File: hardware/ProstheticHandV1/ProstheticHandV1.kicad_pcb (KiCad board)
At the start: 2 copper layers, 119.4 x 88.9 mm, 25 parts, among them J1 Servo_01, J2 Servo_02, J3 Servo_03, J4 Servo_04, J5 JTAG, J6 Bat_Con, J7 OLED_Disp, J8 EMG_Sensor_01, J9 EMG_Sensor_02, SW1 Button_01, SW2 Button_02, U1 LM7805_TO220, U2 LM7809_TO220, U3 LM7909_TO220

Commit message: Done hand PCB v1
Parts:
- moved J6 119.6 mm to (186.4, 79.2), turned to 0 degrees
- moved R7 1.78 mm to (126.7, 113.8)
- moved J3 0.58 mm to (165.4, 78.5)
- moved J4 0.58 mm to (157.7, 78.5)
- moved J1 0.58 mm to (180.6, 78.5)
- moved J2 0.58 mm to (173.0, 78.5)
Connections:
- A2 pad 10: ServoControl_02 -> ServoControl_03
- A2 pad 11: ServoControl_01 -> ServoControl_04
- A2 pad 8: ServoControl_03 -> ServoControl_01
- A2 pad 9: ServoControl_04 -> ServoControl_02
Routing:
- net +BATT: track 64.1 -> 251.8 mm, vias 0 -> 2
- net +5V: track 0.00 -> 155.1 mm, vias 0 -> 2
- net +3V3: track 29.7 -> 181.0 mm, vias 2 -> 4
- net JTAG_TRST: track 0.00 -> 105.8 mm, vias 0 -> 2
- net ServoControl_01: track 0.00 -> 63.5 mm, vias 0 -> 2
- net ServoControl_02: track 0.00 -> 52.8 mm, vias 0 -> 2
- net JTAG_TCK: track 0.00 -> 48.2 mm, vias 0 -> 2
- net ServoControl_03: track 0.00 -> 43.6 mm, vias 0 -> 2
- net JTAG_TDI: track 0.00 -> 37.4 mm, vias 0 -> 2
- net JTAG_TMS: track 0.00 -> 35.3 mm, vias 0 -> 2
- net JTAG_TDO: track 0.00 -> 33.2 mm, vias 0 -> 2
- net ServoControl_04: track 0.00 -> 32.3 mm
- net unconnected-(A2-0-Pad31): track 0.00 -> 9.15 mm
- net unconnected-(A2-19-Pad25): track 0.00 -> 8.90 mm
- net unconnected-(A2-37-Pad34): track 0.00 -> 7.12 mm
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- added copper zone on F.Cu, net GND
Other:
- board size 119.4 x 88.9 mm -> 119.4 x 90.9 mm

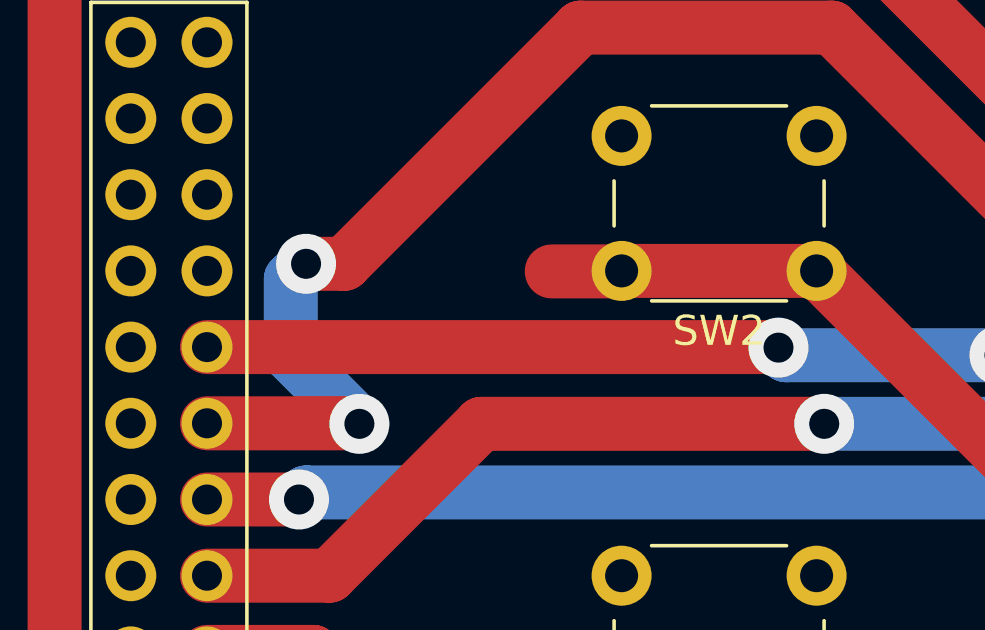
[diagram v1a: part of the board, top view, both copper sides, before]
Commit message: Update schematic: jtag fix
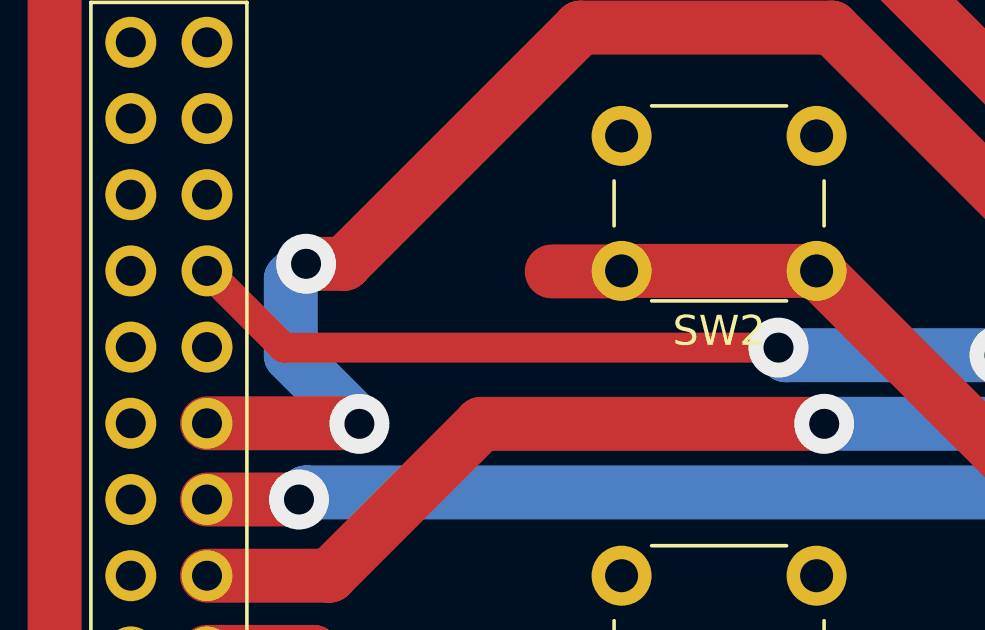
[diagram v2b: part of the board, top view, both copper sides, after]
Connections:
- J5 pad 11: JTAG_TDO -> unconnected-(J5-Pin_11-Pad11)
- J5 pad 13: unconnected-(J5-Pin_13-Pad13) -> JTAG_TDO
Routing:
- net JTAG_TDO: track 33.2 -> 34.3 mm
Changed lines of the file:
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@@
   (net 41 "Net-(D1-A)")
   (net 42 "+BATT")
-  (net 43 "unconnected-(J5-Pin_13-Pad13)")
+  (net 43 "unconnected-(J5-Pin_11-Pad11)")
   (net 44 "unconnected-(J5-Pin_15-Pad15)")
   (net 45 "unconnected-(J5-Pin_17-Pad17)")
@@
       (net 21 "GND") (pinfunction "Pin_10") (pintype "passive"))
     (pad "11" thru_hole oval (at 0 12.7 180) (size 1.7 1.7) (drill 1) (layers "*.Cu" "*.Mask")
-      (net 34 "JTAG_TDO") (pinfunction "Pin_11") (pintype "passive"))
+      (net 43 "unconnected-(J5-Pin_11-Pad11)") (pinfunction "Pin_11") (pintype "passive"))
     (pad "12" thru_hole oval (at 2.54 12.7 180) (size 1.7 1.7) (drill 1) (layers "*.Cu" "*.Mask")
       (net 21 "GND") (pinfunction "Pin_12") (pintype "passive"))
     (pad "13" thru_hole oval (at 0 15.24 180) (size 1.7 1.7) (drill 1) (layers "*.Cu" "*.Mask")
-      (net 43 "unconnected-(J5-Pin_13-Pad13)") (pinfunction "Pin_13") (pintype "passive"))
+      (net 34 "JTAG_TDO") (pinfunction "Pin_13") (pintype "passive"))
     (pad "14" thru_hole oval (at 2.54 15.24 180) (size 1.7 1.7) (drill 1) (layers "*.Cu" "*.Mask")
       (net 21 "GND") (pinfunction "Pin_14") (pintype "passive"))
@@
   (segment (start 100.312 103.36) (end 100.33 103.378) (width 1.8) (layer "F.Cu") (net 34))
   (segment (start 107.968 103.36) (end 107.696 103.632) (width 1.8) (layer "F.Cu") (net 34))
+  (segment (start 81.28 100.82) (end 83.838 103.378) (width 1) (layer "F.Cu") (net 34))
   (segment (start 114.3 103.36) (end 107.968 103.36) (width 1.8) (layer "F.Cu") (net 34))
-  (segment (start 81.28 103.36) (end 100.312 103.36) (width 1.8) (layer "F.Cu") (net 34))
+  (segment (start 83.838 103.378) (end 100.33 103.378) (width 1) (layer "F.Cu") (net 34))
   (via (at 100.33 103.378) (size 2) (drill 1) (layers "F.Cu" "B.Cu") (net 34))
   (via (at 107.696 103.632) (size 2) (drill 1) (layers "F.Cu" "B.Cu") (net 34))

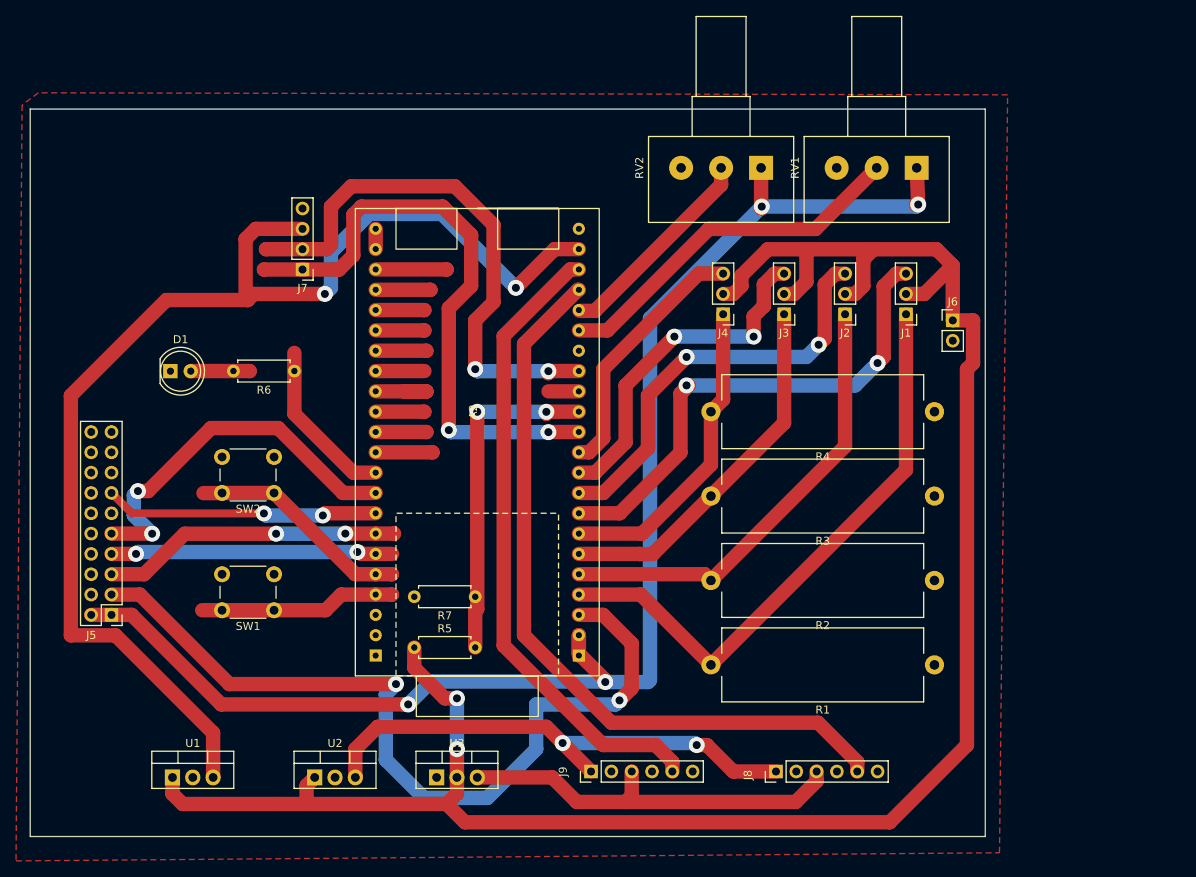
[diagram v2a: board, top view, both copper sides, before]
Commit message: Update PCB for hand, completely new design
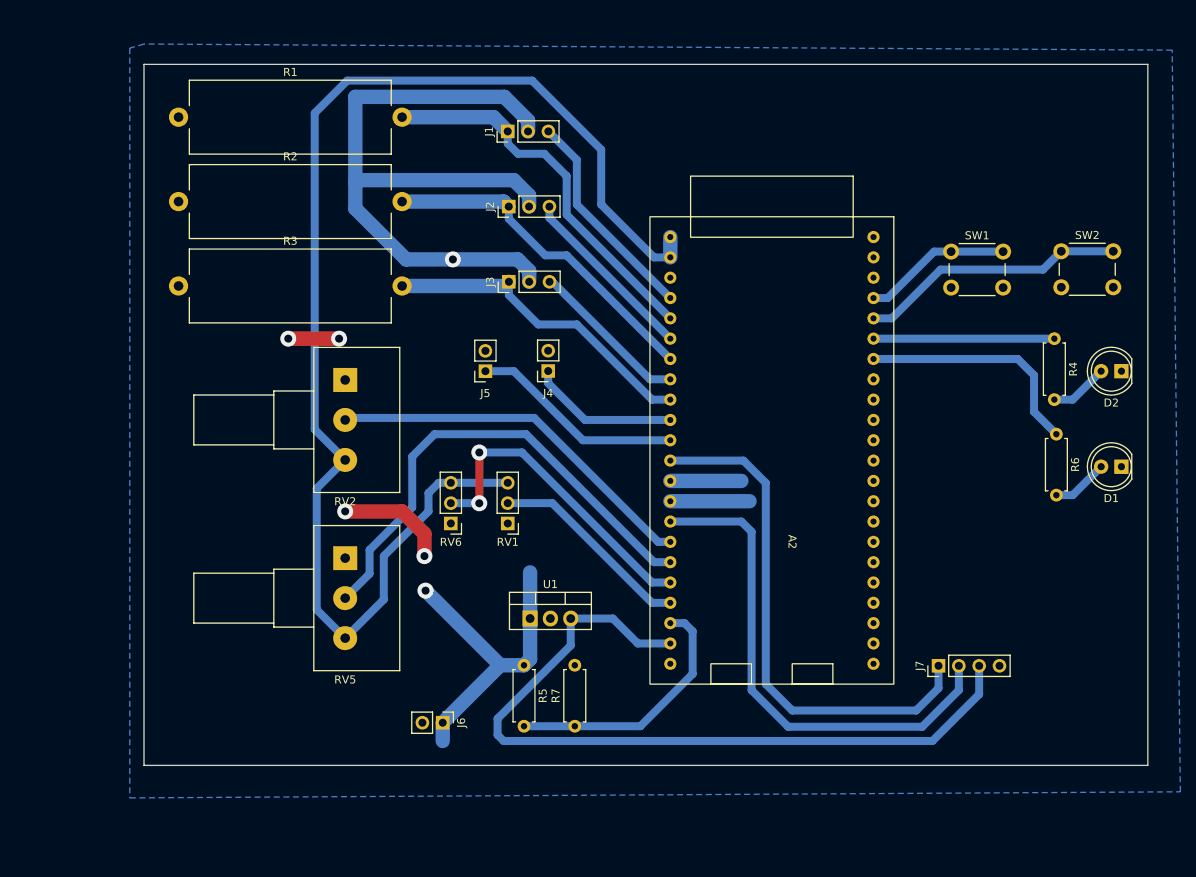
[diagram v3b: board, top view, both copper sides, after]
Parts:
- removed J8: EMG_Sensor_01, Connector_PinHeader_2.54mm:PinHeader_1x06_P2.54mm_Vertical
- removed J9: EMG_Sensor_02, Connector_PinHeader_2.54mm:PinHeader_1x06_P2.54mm_Vertical
- removed U2: LM7809_TO220, Package_TO_SOT_THT:TO-220-3_Vertical
- removed U3: LM7909_TO220, Package_TO_SOT_THT:TO-220-3_Vertical
- added D2: GREEN, LED_THT:LED_D5.0mm, F.Cu at (207.5, 85.6)
- added RV5: TrimPot_02, Potentiometer_THT:Potentiometer_Alps_RK163_Single_Horizontal, F.Cu at (110.5, 109.0)
- added RV6: TrimPot_03, Connector_PinHeader_2.54mm:PinHeader_1x03_P2.54mm_Vertical, F.Cu at (123.7, 104.6)
- A2: footprint MyLibrary:ESP32_S3_DevKitC_V1 -> FootprintLibrary:ESP32S3_DevModule
- J4: value Servo_04 -> EMG_Sensor_01; footprint Connector_PinHeader_2.54mm:PinHeader_1x03_P2.54mm_Vertical -> Connector_PinSocket_2.54mm:PinSocket_1x02_P2.54mm_Vertical
- J5: value JTAG -> EMG_Sensor_02; footprint Connector_PinHeader_2.54mm:PinHeader_2x10_P2.54mm_Vertical -> Connector_PinSocket_2.54mm:PinSocket_1x02_P2.54mm_Vertical
- R4: value 0.1 -> 220; footprint Resistor_THT:R_Axial_Power_L25.0mm_W9.0mm_P27.94mm -> Resistor_THT:R_Axial_DIN0207_L6.3mm_D2.5mm_P7.62mm_Horizontal
- RV1: value TrimPot_01 -> TrimPot_04; footprint Potentiometer_THT:Potentiometer_Alps_RK163_Single_Horizontal -> Connector_PinHeader_2.54mm:PinHeader_1x03_P2.54mm_Vertical
- RV2: value TrimPot_02 -> TrimPot_01
- moved D1 119.5 mm to (207.5, 97.5), turned to 180 degrees
- moved R1 116.7 mm to (89.7, 53.8), turned to 0 degrees
- moved R2 105.7 mm to (89.7, 64.4), turned to 0 degrees
- moved SW2 102.9 mm to (200.0, 70.6), turned to 0 degrees
- moved R3 98.1 mm to (89.7, 74.9), turned to 0 degrees
- moved SW1 95.8 mm to (186.2, 70.6), turned to 0 degrees
- moved R6 95.6 mm to (199.4, 93.5), turned to -90 degrees
- moved J7 93.7 mm to (184.7, 122.4), turned to 90 degrees
- moved J6 81.2 mm to (122.7, 129.5), turned to -90 degrees
- moved RV1 67.7 mm to (130.8, 104.6), turned to 180 degrees
- moved RV2 58.4 mm to (110.5, 86.7), turned to 0 degrees
- moved J5 55.8 mm to (128.0, 85.6)
- moved J1 54.8 mm to (130.8, 55.6), turned to 90 degrees
- moved U1 48.9 mm to (133.6, 116.5)
- moved J2 44.1 mm to (130.9, 65.0), turned to 90 degrees
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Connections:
- A2 pad 10: ServoControl_03 -> EMG_Sensor_01
- A2 pad 11: ServoControl_04 -> EMG_Sensor_02
- A2 pad 13: BattVolt -> unconnected-(A2-3-Pad13)
- A2 pad 16: unconnected-(A2-10-Pad16) -> Pot_01
- A2 pad 17: Pot_01 -> Pot_02
- A2 pad 18: Pot_02 -> Pot_03
- A2 pad 19: EMG_Sensor_01 -> Pot_04
- A2 pad 20: EMG_Sensor_02 -> BattVolt
- A2 pad 3: JTAG_TRST -> unconnected-(A2-RST-Pad3)
- A2 pad 35: DebugLED -> unconnected-(A2-38-Pad35)
- A2 pad 36: JTAG_TCK -> unconnected-(A2-39-Pad36)
- A2 pad 37: JTAG_TDO -> unconnected-(A2-40-Pad37)
- A2 pad 38: JTAG_TDI -> DebugLED_0
- A2 pad 39: JTAG_TMS -> DebugLED_1
- A2 pad 4: ServoCurrSens_01 -> ServoControl_01
- A2 pad 5: ServoCurrSens_02 -> ServoCurrSens_01
- A2 pad 6: ServoCurrSens_03 -> ServoControl_02
- A2 pad 7: ServoCurrSens_04 -> ServoCurrSens_02
- A2 pad 8: ServoControl_01 -> ServoControl_03
- A2 pad 9: ServoControl_02 -> ServoCurrSens_03
- J4 pad 1: ServoCurrSens_04 -> EMG_Sensor_01
- J4 pad 2: +BATT -> GND
- J5 pad 1: +3V3 -> EMG_Sensor_02
- J5 pad 2: +3V3 -> GND
- R4 pad 1: GND -> DebugLED_1
- R4 pad 2: ServoCurrSens_04 -> Net-(D2-A)
- R6 pad 1: DebugLED -> DebugLED_0
- RV1 pad 1: +3V3 -> GND
- RV1 pad 2: Pot_01 -> Pot_04
- RV1 pad 3: GND -> +3V3
- RV2 pad 1: +3V3 -> GND
- RV2 pad 2: Pot_02 -> Pot_01
- RV2 pad 3: GND -> +3V3
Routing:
- net +BATT: track 251.8 -> 129.2 mm
- net JTAG_TRST: track 105.8 -> 0.00 mm, vias 2 -> 0
- net EMG_Sensor_01: track 95.5 -> 18.7 mm
- net +9V: track 64.9 -> 0.00 mm, vias 2 -> 0
- net +5V: track 155.1 -> 98.6 mm, vias 2 -> 0
- net EMG_Sensor_02: track 79.8 -> 26.7 mm
- net -9V: track 50.1 -> 0.00 mm
- net JTAG_TCK: track 48.2 -> 0.00 mm, vias 2 -> 0
- net Pot_03: track 0.00 -> 40.5 mm, vias 0 -> 2
- net ServoCurrSens_04: track 39.5 -> 0.00 mm
- net JTAG_TDI: track 37.4 -> 0.00 mm, vias 2 -> 0
- net ServoControl_01: track 63.5 -> 27.1 mm, vias 2 -> 0
- net JTAG_TMS: track 35.3 -> 0.00 mm, vias 2 -> 0
- net Pot_02: track 26.3 -> 61.2 mm
- net JTAG_TDO: track 34.3 -> 0.00 mm, vias 2 -> 0
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- added copper zone on B.Cu, net GND
- removed copper zone on F.Cu, net GND
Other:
- board size 119.4 x 90.9 mm -> 125.5 x 87.6 mm

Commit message: Update code in main branch a bit
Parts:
- added SW3: SW_Boostrap, Button_Switch_THT:SW_DIP_SPSTx04_Slide_9.78x12.34mm_W7.62mm_P2.54mm, F.Cu at (198.6, 83.8)
- moved R6 19.1 mm to (199.6, 112.5)
- moved D1 19.1 mm to (207.8, 116.6)
- moved D2 19.1 mm to (207.8, 104.6)
- moved R4 19.1 mm to (199.4, 100.6)
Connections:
- A2 pad 34: unconnected-(A2-37-Pad34) -> DebugLED_0
- A2 pad 35: unconnected-(A2-38-Pad35) -> DebugLED_1
- A2 pad 36: unconnected-(A2-39-Pad36) -> Boostrap_03
- A2 pad 37: unconnected-(A2-40-Pad37) -> Boostrap_02
- A2 pad 38: DebugLED_0 -> Boostrap_01
- A2 pad 39: DebugLED_1 -> Boostrap_00
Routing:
- net Boostrap_03: track 0.00 -> 23.0 mm
- net Boostrap_02: track 0.00 -> 23.0 mm
- net Boostrap_01: track 0.00 -> 23.0 mm
- net Boostrap_00: track 0.00 -> 23.0 mm
- net DebugLED_0: track 29.4 -> 33.7 mm
- net DebugLED_1: track 22.6 -> 26.5 mm
- net ServoControl_02: track 22.8 -> 24.3 mm
- net ServoControl_01: track 27.1 -> 28.6 mm
- net ServoCurrSens_01: track 47.7 -> 49.2 mm
- net +3V3: track 164.9 -> 165.6 mm

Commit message: Update button driver and schematic names
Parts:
- SW3: value SW_Boostrap -> SW_Bootstrap
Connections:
- net Boostrap_00 renamed Bootstrap_00
- net Boostrap_01 renamed Bootstrap_01
- net Boostrap_02 renamed Bootstrap_02
- net Boostrap_03 renamed Bootstrap_03
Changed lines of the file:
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@@
   (net 29 "unconnected-(A2-35-Pad32)")
   (net 30 "unconnected-(A2-36-Pad33)")
-  (net 31 "Boostrap_03")
-  (net 32 "Boostrap_02")
-  (net 33 "Boostrap_01")
-  (net 34 "Boostrap_00")
+  (net 31 "Bootstrap_03")
+  (net 32 "Bootstrap_02")
+  (net 33 "Bootstrap_01")
+  (net 34 "Bootstrap_00")
   (net 35 "DebugLED_0")
   (net 36 "DebugLED_1")
@@
         (effects (font (size 1 1) (thickness 0.15)))
     )
-    (fp_text value "SW_Boostrap" (at 3.81 11.04) (layer "F.Fab")
+    (fp_text value "SW_Bootstrap" (at 3.81 11.04) (layer "F.Fab")
         (effects (font (size 1 1) (thickness 0.15)))
     )
@@
       (stroke (width 0.1) (type solid)) (layer "F.Fab"))
     (pad "1" thru_hole rect (at 0 0) (size 1.6 1.6) (drill 0.8) (layers "*.Cu" "*.Mask")
-      (net 34 "Boostrap_00") (pintype "passive"))
+      (net 34 "Bootstrap_00") (pintype "passive"))
     (pad "2" thru_hole oval (at 0 2.54) (size 1.6 1.6) (drill 0.8) (layers "*.Cu" "*.Mask")
-      (net 33 "Boostrap_01") (pintype "passive"))
+      (net 33 "Bootstrap_01") (pintype "passive"))
     (pad "3" thru_hole oval (at 0 5.08) (size 1.6 1.6) (drill 0.8) (layers "*.Cu" "*.Mask")
-      (net 32 "Boostrap_02") (pintype "passive"))
+      (net 32 "Bootstrap_02") (pintype "passive"))
     (pad "4" thru_hole oval (at 0 7.62) (size 1.6 1.6) (drill 0.8) (layers "*.Cu" "*.Mask")
-      (net 31 "Boostrap_03") (pintype "passive"))
+      (net 31 "Bootstrap_03") (pintype "passive"))
     (pad "5" thru_hole oval (at 7.62 7.62) (size 1.6 1.6) (drill 0.8) (layers "*.Cu" "*.Mask")
       (net 21 "GND") (pintype "passive"))
@@
       (net 36 "DebugLED_1") (pinfunction "38") (pintype "bidirectional"))
     (pad "36" thru_hole circle (at -7.62 -12.7 270) (size 1.524 1.524) (drill 0.762) (layers "*.Cu" "*.Mask")
-      (net 31 "Boostrap_03") (pinfunction "39") (pintype "bidirectional"))
+      (net 31 "Bootstrap_03") (pinfunction "39") (pintype "bidirectional"))
     (pad "37" thru_hole circle (at -10.16 -12.7 270) (size 1.524 1.524) (drill 0.762) (layers "*.Cu" "*.Mask")
-      (net 32 "Boostrap_02") (pinfunction "40") (pintype "bidirectional"))
+      (net 32 "Bootstrap_02") (pinfunction "40") (pintype "bidirectional"))
     (pad "38" thru_hole circle (at -12.7 -12.7 270) (size 1.524 1.524) (drill 0.762) (layers "*.Cu" "*.Mask")
-      (net 33 "Boostrap_01") (pinfunction "41") (pintype "bidirectional"))
+      (net 33 "Bootstrap_01") (pinfunction "41") (pintype "bidirectional"))
     (pad "39" thru_hole circle (at -15.24 -12.7 270) (size 1.524 1.524) (drill 0.762) (layers "*.Cu" "*.Mask")
-      (net 34 "Boostrap_00") (pinfunction "42") (pintype "bidirectional"))
+      (net 34 "Bootstrap_00") (pinfunction "42") (pintype "bidirectional"))
     (pad "40" thru_hole circle (at -17.78 -12.7 270) (size 1.524 1.524) (drill 0.762) (layers "*.Cu" "*.Mask")
       (net 37 "Button_02") (pinfunction "2") (pintype "bidirectional"))
